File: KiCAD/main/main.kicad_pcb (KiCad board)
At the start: 2 copper layers, 52.1 x 53.3 mm, 16 parts, among them IC1 DHT22, J1 Charge Controller, J2 Sound Sensor, J3 BuckConverter, J4 Anemometer, J5 Conn_02x04_Odd_Even, SW1 BOOT, SW2 RESET, U1 ESP32-WROOM-32

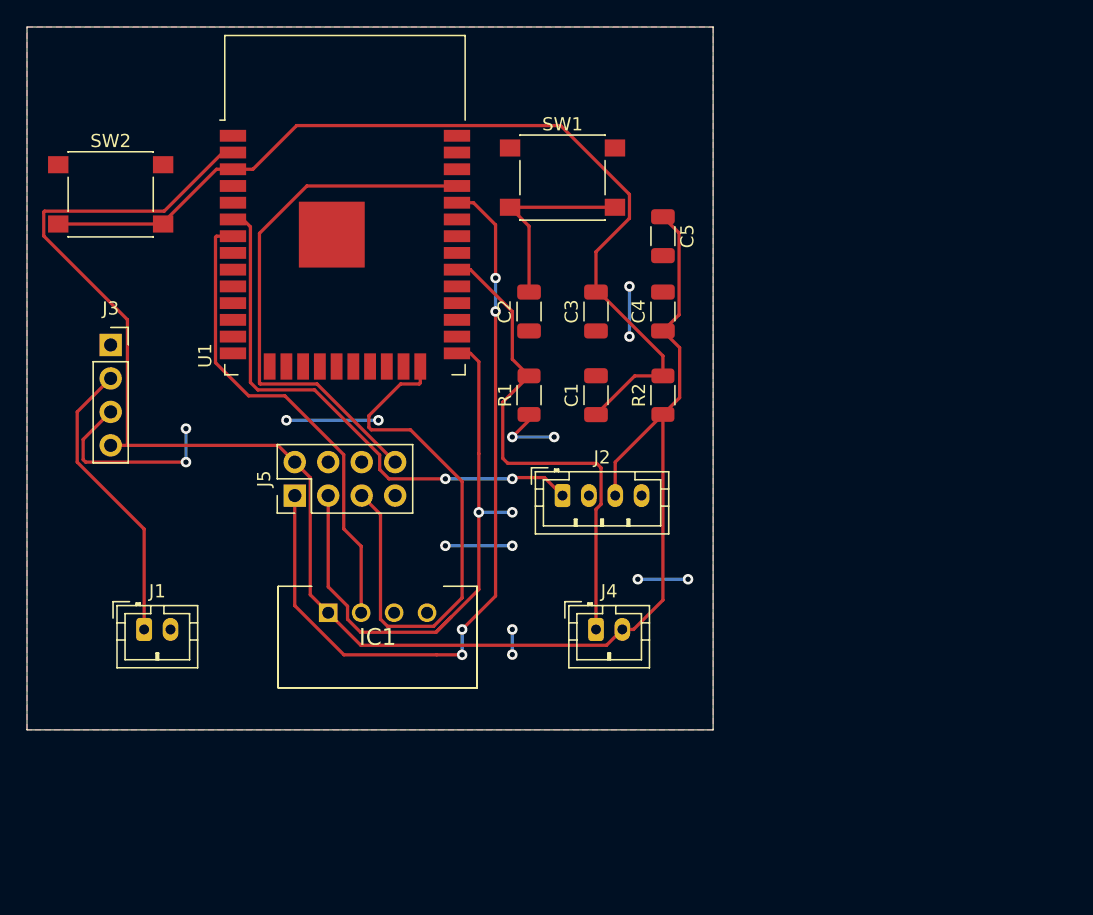
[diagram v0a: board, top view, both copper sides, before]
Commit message: Better track size and all connections done on preliminary pcb
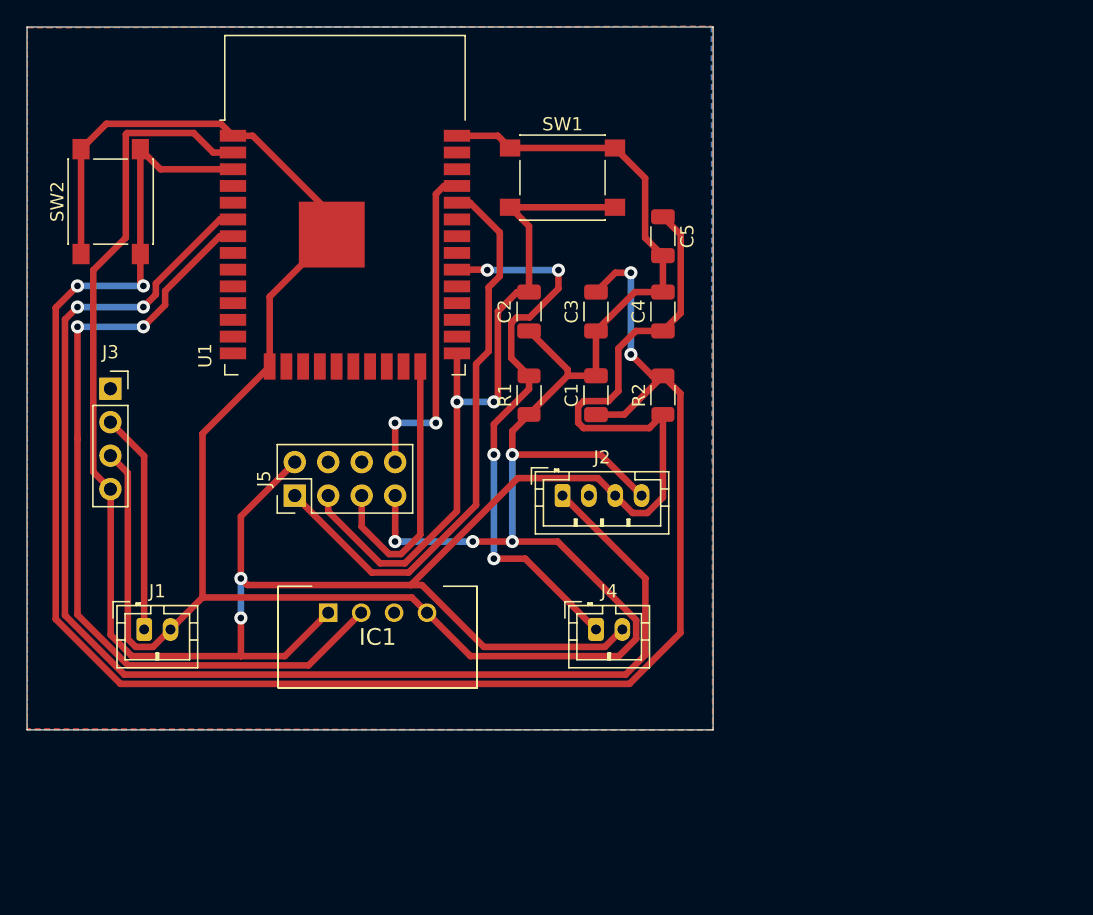
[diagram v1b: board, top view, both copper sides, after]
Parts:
- moved J3 3.32 mm to (96.5, 84.6)
- moved SW2 0.55 mm to (96.5, 70.4), turned to 90 degrees
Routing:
- net GND: track 41.9 -> 213.4 mm, vias 14 -> 4
- net /Microcontroller/EN: track 72.0 -> 139.1 mm, vias 0 -> 4
- net /Sound_Signal: track 41.3 -> 100.1 mm
- net +3V3: track 130.2 -> 174.1 mm, vias 0 -> 2
- net /DHT22_Data: track 36.0 -> 61.9 mm, vias 0 -> 2
- net /Microcontroller/IO2: track 42.0 -> 21.1 mm
- net /Microcontroller/RXD0: track 59.9 -> 43.9 mm, vias 4 -> 0
- net /Microcontroller/TXD0: track 40.6 -> 25.3 mm, vias 0 -> 2
- net /Microcontroller/IO0: track 60.1 -> 54.0 mm
- net /Vin_Buck: track 22.2 -> 16.8 mm
- net /Anemometer_Out: track 38.2 -> 43.3 mm, vias 0 -> 4
- added copper zone on B.Cu, net (none)
- added copper zone on F.Cu, net (none)
- removed copper zone on F.Cu, net GND
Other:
- net class Default: trace_width 0.25 -> 0.5
- rule trace_min: 0.2 -> 0.5

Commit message: Preliminary layout with fixed component pins
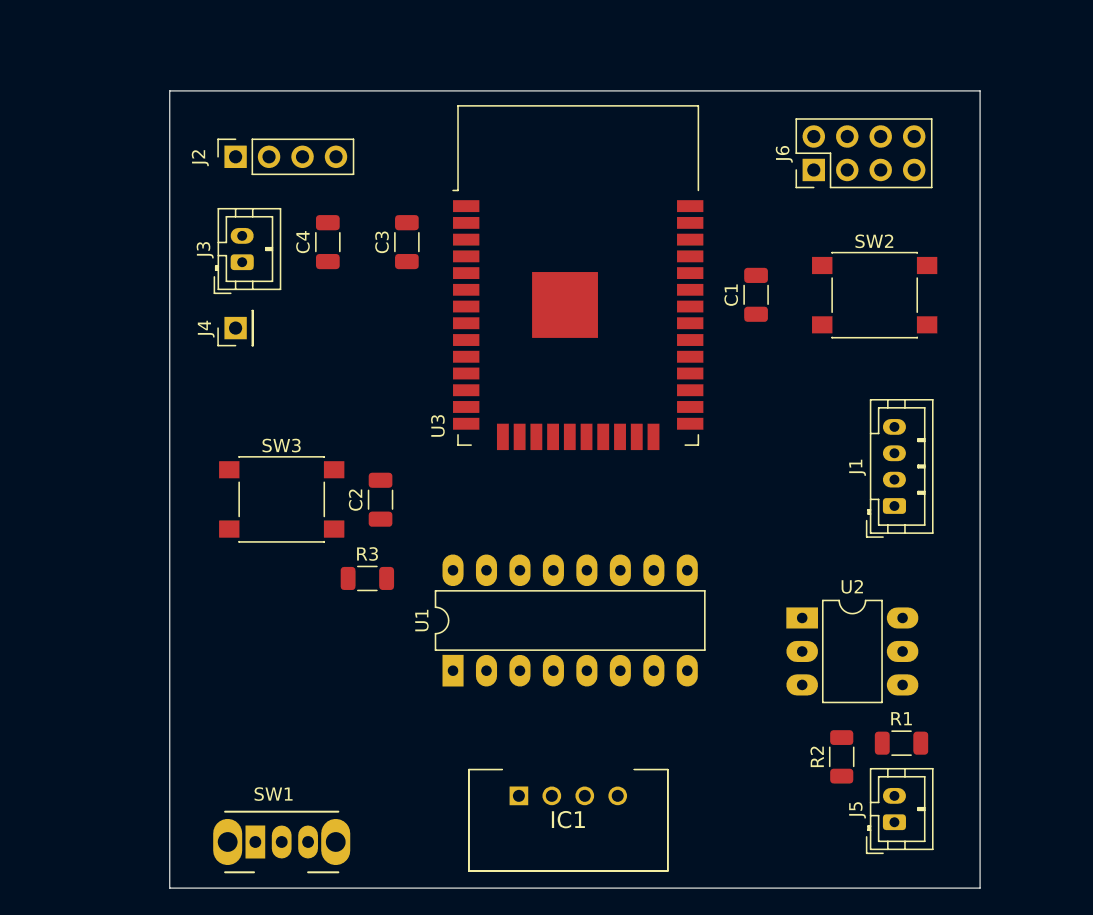
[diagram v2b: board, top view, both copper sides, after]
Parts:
- removed C5: 0.1uF, Capacitor_SMD:C_1206_3216Metric
- added J6: Conn_02x04_Odd_Even, Connector_PinHeader_2.54mm:PinHeader_2x04_P2.54mm_Vertical, F.Cu at (149.9, 68.0)
- added R3: 10kR, Resistor_SMD:R_1206_3216Metric, F.Cu at (116.0, 99.0)
- added SW3: RESET, Button_Switch_SMD:SW_SPST_PTS645, F.Cu at (109.5, 93.0)
- added U2: 4N25, Package_DIP:DIP-6_W7.62mm_LongPads, F.Cu at (149.0, 102.0)
- added U3: ESP32-WROOM-32, RF_Module:ESP32-WROOM-32, F.Cu at (132.0, 79.0)
- C3: value 0.1uF -> 22uF
- C4: value 22uF -> 0.1uF
- J1: value Charge Controller -> Sound Sensor; footprint Connector_JST:JST_PH_B2B-PH-K_1x02_P2.00mm_Vertical -> Connector_JST:JST_PH_B4B-PH-K_1x04_P2.00mm_Vertical
- J2: value Sound Sensor -> BuckConverter; footprint Connector_JST:JST_PH_B4B-PH-K_1x04_P2.00mm_Vertical -> Connector_PinSocket_2.54mm:PinSocket_1x04_P2.54mm_Vertical
- J3: value BuckConverter -> Charge Controller; footprint Connector_PinSocket_2.54mm:PinSocket_1x04_P2.54mm_Vertical -> Connector_JST:JST_PH_B2B-PH-K_1x02_P2.00mm_Vertical
- J4: value Anemometer -> Battery Status; footprint Connector_JST:JST_PH_B2B-PH-K_1x02_P2.00mm_Vertical -> Connector_PinHeader_2.54mm:PinHeader_1x01_P2.54mm_Vertical
- J5: value Conn_02x04_Odd_Even -> Anemometer; footprint Connector_PinHeader_2.54mm:PinHeader_2x04_P2.54mm_Vertical -> Connector_JST:JST_PH_B2B-PH-K_1x02_P2.00mm_Vertical
- R1: value R -> 10k
- R2: value 10kR -> 620
- SW1: value BOOT -> SW_SPDT; footprint Button_Switch_SMD:SW_SPST_PTS645 -> Button_Switch_THT:SW_CuK_OS102011MA1QN1_SPDT_Angled
- SW2: value RESET -> BOOT
- U1: value ESP32-WROOM-32 -> 4020; footprint RF_Module:ESP32-WROOM-32 -> Package_DIP:DIP-16_W7.62mm_LongPads
- moved SW2 58.4 mm to (154.5, 77.5), turned to 0 degrees
- moved J1 57.7 mm to (156.0, 93.5), turned to 90 degrees
- moved SW1 55.5 mm to (107.5, 119.0)
- moved J5 51.8 mm to (156.0, 117.5)
- moved R1 38.7 mm to (156.5, 111.5), turned to 0 degrees
- moved J2 35.7 mm to (106.0, 67.0), turned to 90 degrees
- moved J4 35.7 mm to (106.0, 80.0), turned to 90 degrees
- moved U1 33.4 mm to (122.5, 106.0), turned to 90 degrees
- moved R2 30.6 mm to (152.0, 112.5)
- moved C4 26.0 mm to (113.0, 73.5)
- moved IC1 20.1 mm to (127.5, 115.5)
- moved C2 18.2 mm to (117.0, 93.0)
- moved C3 15.3 mm to (119.0, 73.5)
- moved C1 14.3 mm to (145.5, 77.5)
- moved J3 13.9 mm to (106.5, 75.0), turned to 90 degrees
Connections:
- C1 pad 1: /Microcontroller/EN -> /Microcontroller/IO0
- C2 pad 1: GND -> /Microcontroller/EN
- C2 pad 2: /Microcontroller/IO0 -> GND
- C3 pad 1: GND -> +3V3
- C3 pad 2: /Microcontroller/EN -> GND
- IC1 pad 1: +3V3 -> /supply_on
- J1 pad 1: /Vin_Buck -> /Sound_Signal
- J1 pad 2: GND -> Net-(J1-Pad2)
- J2 pad 1: /Sound_Signal -> Net-(J2-Pad1)
- J2 pad 2: Net-(J2-Pad2) -> /Vin_Buck
- J2 pad 3: +3V3 -> GND
- J2 pad 4: GND -> +3V3
- J3 pad 2: /Vin_Buck -> GND
- J4 pad 1: /Anemometer_Out -> /Battery_status
- J5 pad 1: /Microcontroller/RXD0 -> /Anemometer_Out
- R1 pad 2: /Anemometer_Out -> /Opto_Anemometer_Out
- R2 pad 1: +3V3 -> /Anemometer_Out
- R2 pad 2: /Microcontroller/EN -> Net-(R2-Pad2)
- SW1 pad 1: GND -> /Vin_Buck
- SW1 pad 2: /Microcontroller/IO0 -> Net-(J3-Pad1)
- SW2 pad 2: /Microcontroller/EN -> /Microcontroller/IO0
- U1 pad 1: GND -> /Microcontroller/IO27
- U1 pad 10: /Microcontroller/IO25 -> /Opto_Anemometer_Out
- U1 pad 11: /Microcontroller/IO26 -> /reset_counter
- U1 pad 12: /Microcontroller/IO27 -> /Microcontroller/IO23
- U1 pad 13: /Microcontroller/IO14 -> /Microcontroller/IO22
- U1 pad 14: /Microcontroller/IO12 -> /Microcontroller/IO25
- U1 pad 15: GND -> /Microcontroller/IO26
- U1 pad 16: /Microcontroller/IO13 -> +3V3
- U1 pad 2: +3V3 -> /Microcontroller/IO32
- U1 pad 3: /Microcontroller/EN -> /Microcontroller/IO33
- U1 pad 4: /Microcontroller/SENSOR_VP -> /Microcontroller/IO19
- U1 pad 5: /Microcontroller/SENSOR_VN -> /Microcontroller/IO18
- U1 pad 6: /Sound_Signal -> /Microcontroller/I021
- U1 pad 7: /DHT22_Data -> /Microcontroller/IO17
- U1 pad 8: /Microcontroller/IO32 -> GND
- U1 pad 9: /Microcontroller/IO33 -> /Microcontroller/IO16
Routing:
- net GND: track 213.4 -> 0.00 mm, vias 4 -> 0
- net +3V3: track 174.1 -> 0.00 mm, vias 2 -> 0
- net /Microcontroller/EN: track 139.1 -> 0.00 mm, vias 4 -> 0
- net /Sound_Signal: track 100.1 -> 0.00 mm, vias 2 -> 0
- net /DHT22_Data: track 61.9 -> 0.00 mm, vias 2 -> 0
- net /Microcontroller/IO0: track 54.0 -> 0.00 mm, vias 2 -> 0
- net /Microcontroller/RXD0: track 43.9 -> 0.00 mm
- net /Anemometer_Out: track 43.3 -> 0.00 mm, vias 4 -> 0
- net /Microcontroller/TXD0: track 25.3 -> 0.00 mm, vias 2 -> 0
- net /Microcontroller/IO2: track 21.1 -> 0.00 mm
- net /Vin_Buck: track 16.8 -> 0.00 mm
- removed copper zone on B.Cu, net (none)
- removed copper zone on F.Cu, net (none)
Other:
- board size 52.1 x 53.3 mm -> 61.5 x 60.5 mm

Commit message: All connections done
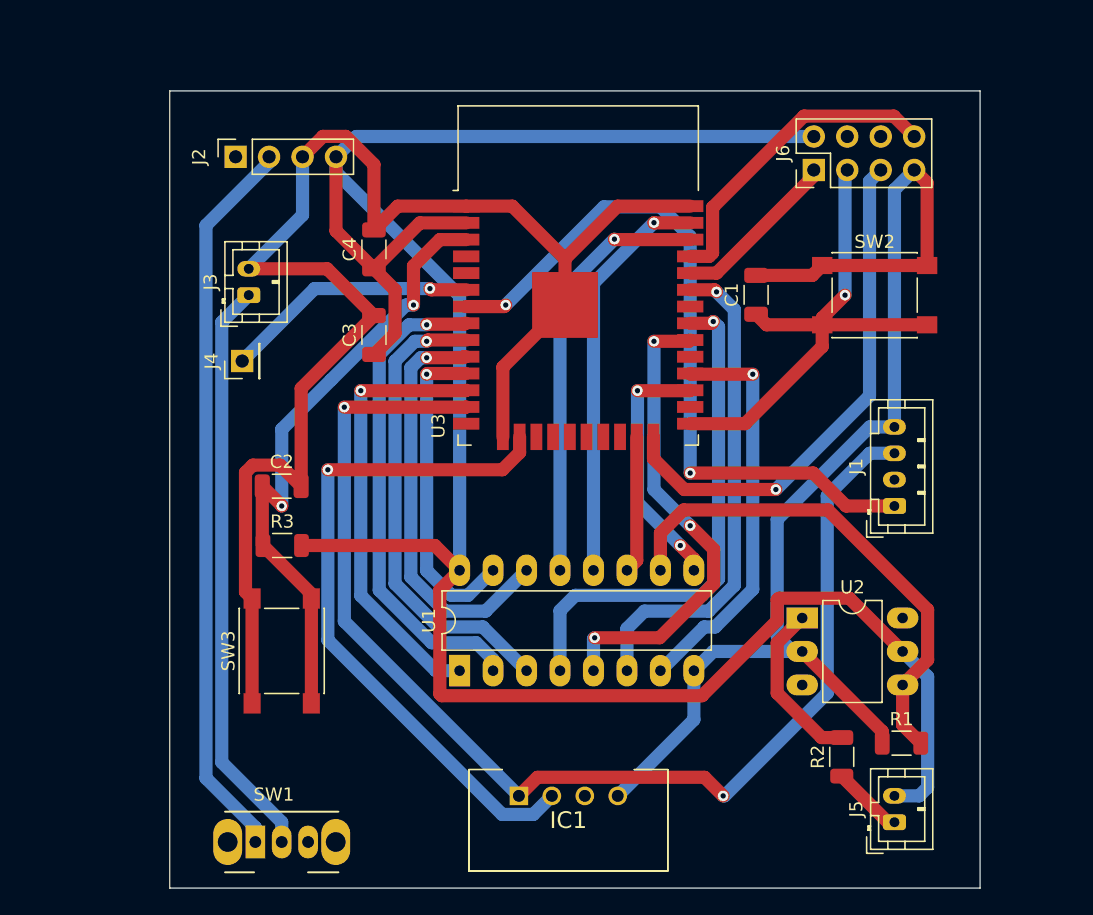
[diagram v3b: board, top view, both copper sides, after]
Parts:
- moved SW3 11.5 mm to (109.5, 104.5), turned to 90 degrees
- moved C2 7.57 mm to (109.5, 92.0), turned to 0 degrees
- moved C3 7.48 mm to (116.5, 80.5)
- moved R3 6.93 mm to (109.5, 96.5)
- moved C4 3.54 mm to (116.5, 74.0)
- moved J3 2.55 mm to (107.0, 77.5)
- moved J4 2.55 mm to (106.5, 82.5)
- moved U1 0.50 mm to (123.0, 106.0)
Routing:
- net GND: track 0.00 -> 209.0 mm
- net +3V3: track 0.00 -> 175.6 mm
- net /supply_on: track 0.00 -> 93.5 mm, vias 0 -> 2
- net /Sound_Signal: track 0.00 -> 55.5 mm, vias 0 -> 2
- net /Vin_Buck: track 0.00 -> 55.5 mm
- net /DHT22_Data: track 0.00 -> 52.3 mm, vias 0 -> 1
- net /Microcontroller/EN: track 0.00 -> 47.7 mm, vias 0 -> 2
- net Net-(J3-Pad1): track 0.00 -> 44.2 mm
- net /Microcontroller/IO0: track 0.00 -> 39.9 mm, vias 0 -> 1
- net /Microcontroller/IO2: track 0.00 -> 39.5 mm, vias 0 -> 1
- net /Microcontroller/IO19: track 0.00 -> 39.1 mm, vias 0 -> 1
- net /Opto_Anemometer_Out: track 0.00 -> 38.4 mm
- net /Microcontroller/I021: track 0.00 -> 37.6 mm, vias 0 -> 1
- net /Microcontroller/IO32: track 0.00 -> 37.1 mm, vias 0 -> 1
- net /Microcontroller/IO18: track 0.00 -> 36.3 mm, vias 0 -> 3
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
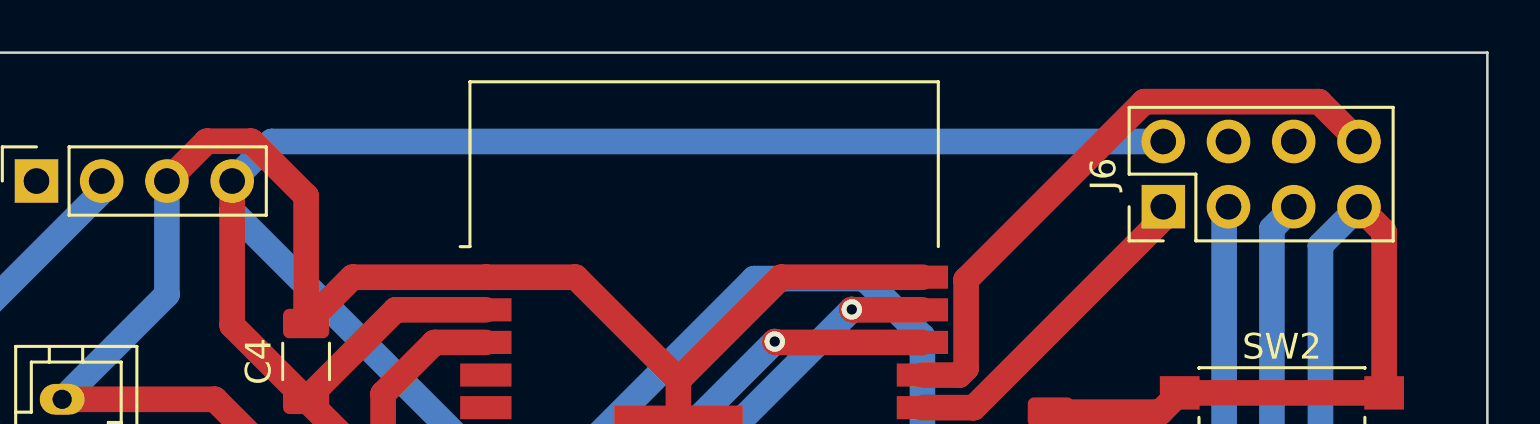
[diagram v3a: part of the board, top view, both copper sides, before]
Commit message: Add unconnected GND
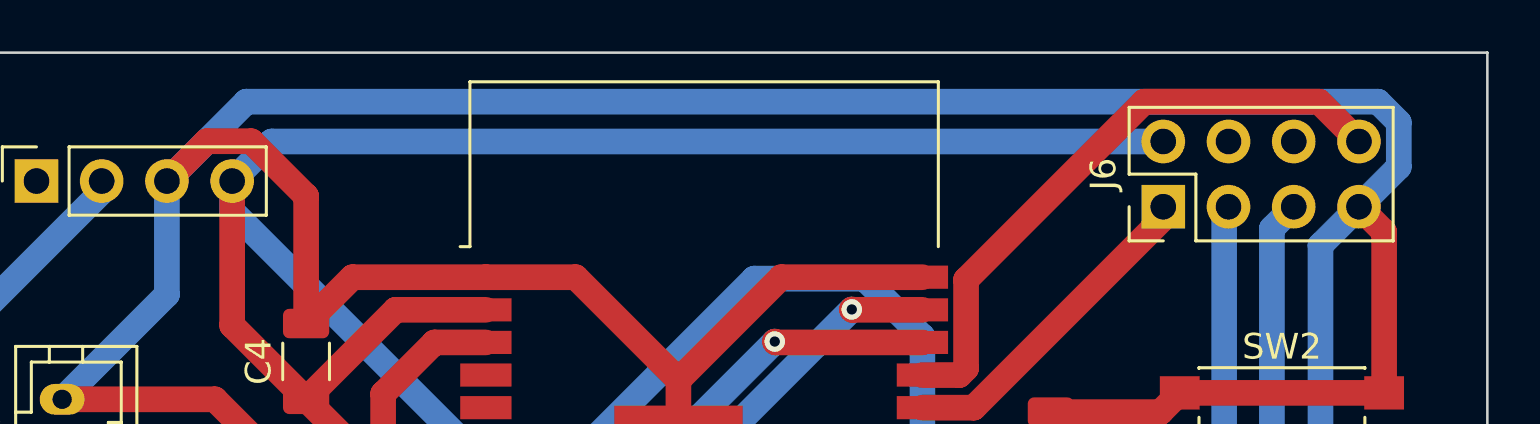
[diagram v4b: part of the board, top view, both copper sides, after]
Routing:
- net GND: track 209.0 -> 262.5 mm
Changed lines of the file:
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@@
     (thickness 1.6)
     (drawings 4)
-    (tracks 275)
+    (tracks 280)
     (zones 0)
     (modules 20)
@@
   (segment (start 116.5 67.585998) (end 114.364001 65.449999) (width 1) (layer F.Cu) (net 1))
   (segment (start 116.5 72.55) (end 116.5 67.585998) (width 1) (layer F.Cu) (net 1))
+  (segment (start 159.050001 66.449999) (end 157.5 68) (width 1) (layer B.Cu) (net 1))
+  (segment (start 158.244001 63.909999) (end 159.050001 64.715999) (width 1) (layer B.Cu) (net 1))
+  (segment (start 159.050001 64.715999) (end 159.050001 66.449999) (width 1) (layer B.Cu) (net 1))
+  (segment (start 114.170001 63.909999) (end 158.244001 63.909999) (width 1) (layer B.Cu) (net 1))
+  (segment (start 111.08 67) (end 114.170001 63.909999) (width 1) (layer B.Cu) (net 1))
   (segment (start 108.025 96.45) (end 108.075 96.5) (width 1) (layer F.Cu) (net 2))
   (segment (start 108.025 92) (end 108.025 96.45) (width 1) (layer F.Cu) (net 2))

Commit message: Preliminary final PCB
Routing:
- added copper zone on B.Cu, net (none)
- added copper zone on F.Cu, net (none)
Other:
- net class Default: trace_width 0.5 -> 1; via_dia 0.8 -> 1.2; via_drill 0.4 -> 0.8
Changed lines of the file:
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@@
     (zone_45_only no)
     (trace_min 0.5)
-    (via_size 0.8)
-    (via_drill 0.4)
+    (via_size 1.2)
+    (via_drill 0.8)
     (via_min_size 0.4)
     (via_min_drill 0.3)
@@
   (net_class Default "This is the default net class."
     (clearance 0.2)
-    (trace_width 0.5)
-    (via_dia 0.8)
-    (via_drill 0.4)
+    (trace_width 1)
+    (via_dia 1.2)
+    (via_drill 0.8)
     (uvia_dia 0.3)
     (uvia_drill 0.1)
@@
   (segment (start 136.445 97.635) (end 136.445 88.255) (width 1) (layer F.Cu) (net 38))
   (segment (start 135.7 98.38) (end 136.445 97.635) (width 1) (layer F.Cu) (net 38))
+  (zone (net 0) (net_name "") (layer F.Cu) (hatch edge 0.508)
+    (connect_pads (clearance 0.508))
+    (min_thickness 0.254)
+    (fill yes (arc_segments 32) (thermal_gap 0.508) (thermal_bridge_width 0.508))
+    (polygon
+      (pts
+        (xy 162.5 122.5) (xy 101 122.5) (xy 101 62) (xy 162.5 62)
+      )
+    )
+  )
+  (zone (net 0) (net_name "") (layer B.Cu) (hatch edge 0.508)
+    (connect_pads (clearance 0.508))
+    (min_thickness 0.254)
+    (fill yes (arc_segments 32) (thermal_gap 0.508) (thermal_bridge_width 0.508))
+    (polygon
+      (pts
+        (xy 162.5 122.5) (xy 101 122.5) (xy 101 62) (xy 162.5 62)
+      )
+    )
+  )
 )
